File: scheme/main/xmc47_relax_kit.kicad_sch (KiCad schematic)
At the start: 0 parts

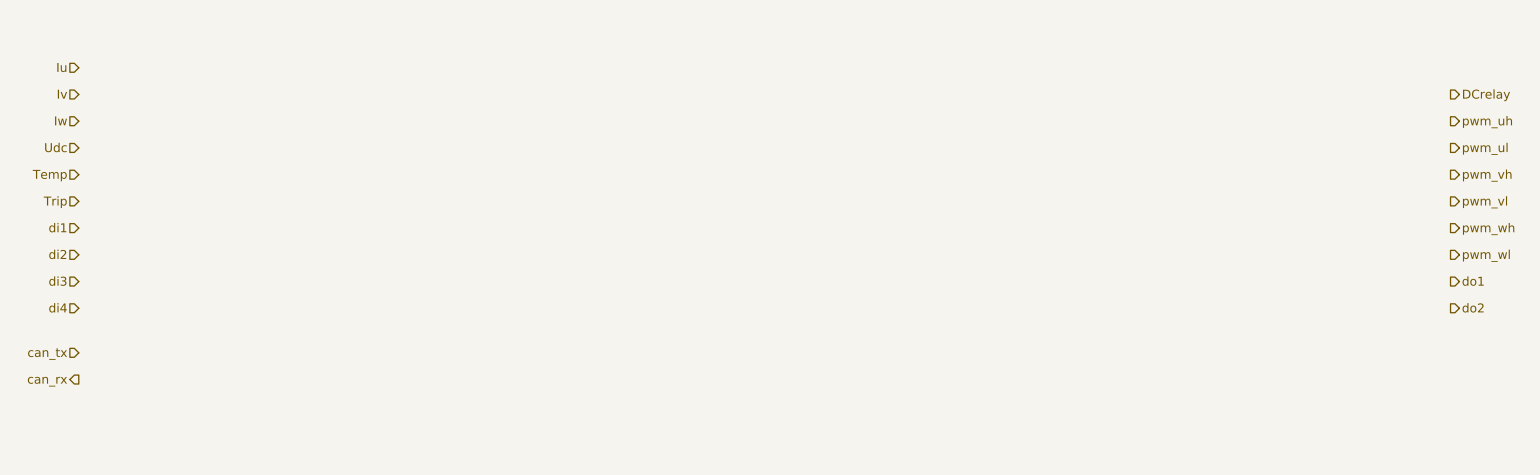
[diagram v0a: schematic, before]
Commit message: KIT_XMC45_RELAX_V1 symbol
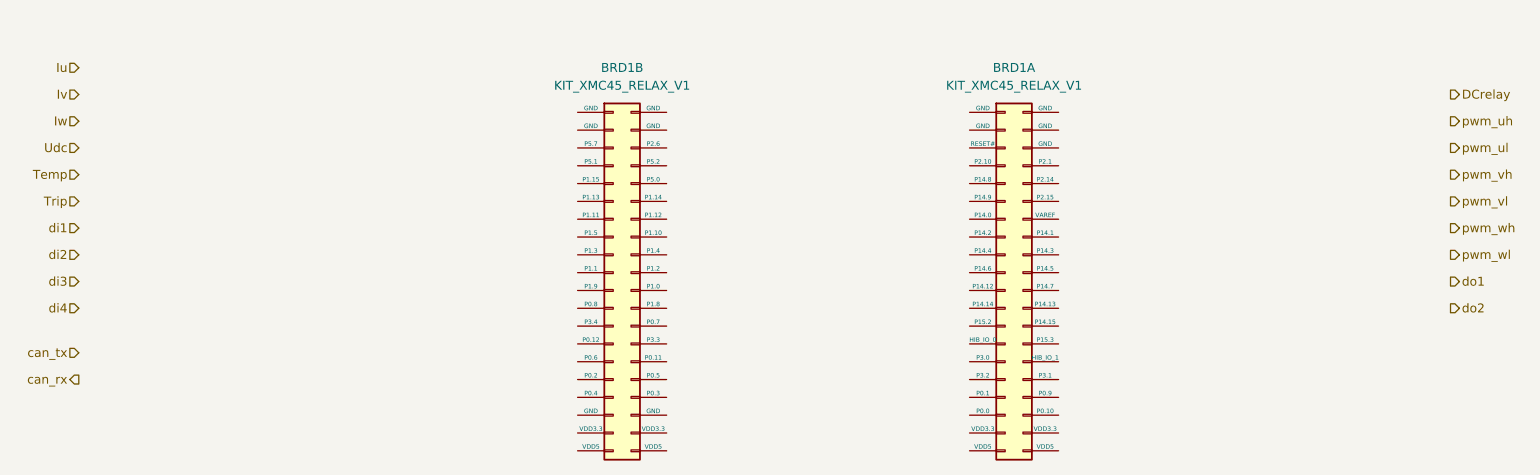
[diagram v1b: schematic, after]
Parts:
- added BRD1: KIT_XMC45_RELAX_V1, symbol main:KIT_XMC45_RELAX_V1

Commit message: KIT_XMC47_RELAX_V1 symbol
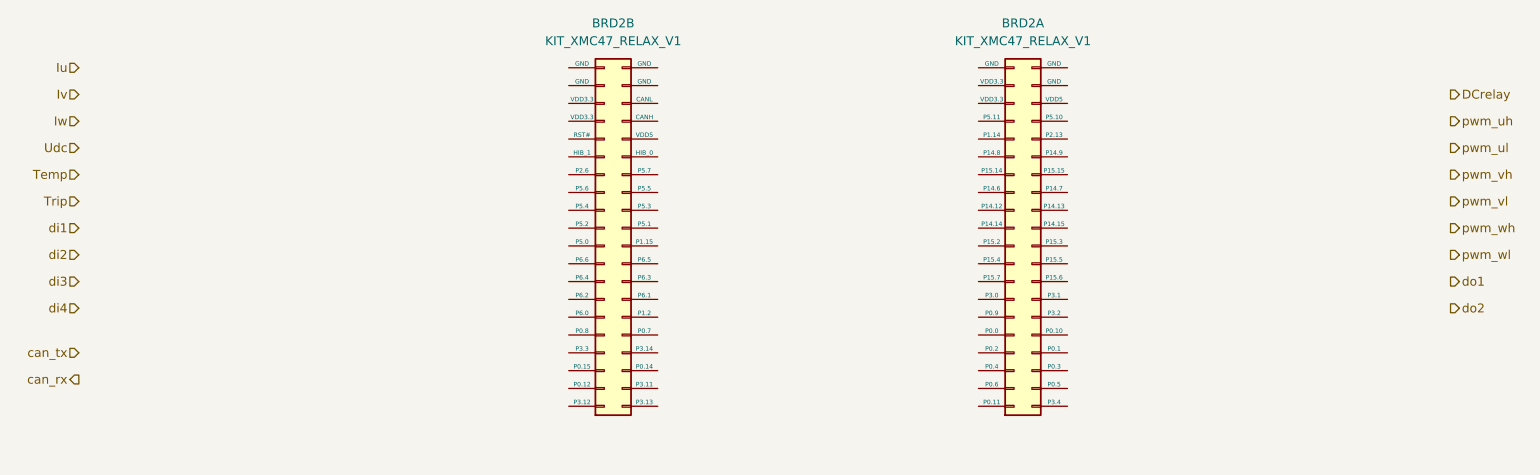
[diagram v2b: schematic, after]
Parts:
- removed BRD1: KIT_XMC45_RELAX_V1, symbol main:KIT_XMC45_RELAX_V1
- added BRD2: KIT_XMC47_RELAX_V1, symbol main:KIT_XMC47_RELAX_V1
